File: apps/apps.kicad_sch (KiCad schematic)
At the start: 12 parts, among them J1 Conn_OUTPUT, Q1 SS9013, U1 XTR117

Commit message: chore: change XTR117 footprint
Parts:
- U1: footprint Package_SO:SOIC-8_3.9x4.9mm_P1.27mm -> Package_SO:VSSOP-8_3.0x3.0mm_P0.65mm
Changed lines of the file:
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@@
       (effects (font (size 1.27 1.27)))
     )
-    (property "Footprint" "Package_SO:SOIC-8_3.9x4.9mm_P1.27mm" (at 67.31 55.88 0)
+    (property "Footprint" "Package_SO:VSSOP-8_3.0x3.0mm_P0.65mm" (at 67.31 55.88 0)
       (effects (font (size 1.27 1.27)) hide)
     )

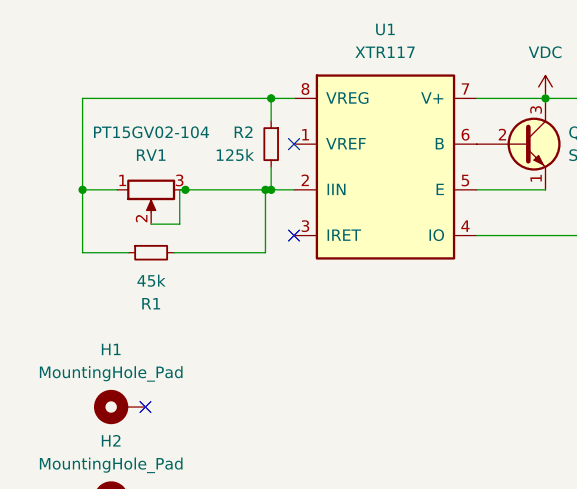
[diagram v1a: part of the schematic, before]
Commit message: fix: update resistor
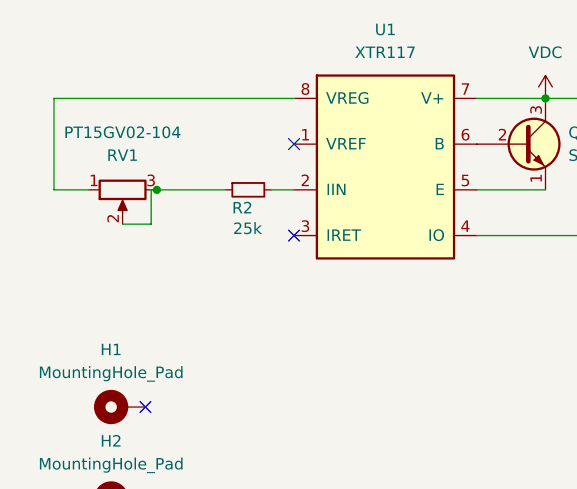
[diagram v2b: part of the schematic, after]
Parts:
- removed R1: 45k, Resistor_SMD:R_0603_1608Metric, symbol Device:R_Small
- R2: value 125k -> 25k
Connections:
- net at RV1.1, U1.8 (VREG): no longer R2.1
- net at RV1.2, RV1.3: now also R2.1; no longer R2.2, U1.2 (IIN)
- new net: R2.2, U1.2 (IIN)
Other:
- moved on the sheet: R2, RV1
